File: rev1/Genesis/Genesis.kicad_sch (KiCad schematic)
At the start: 0 parts

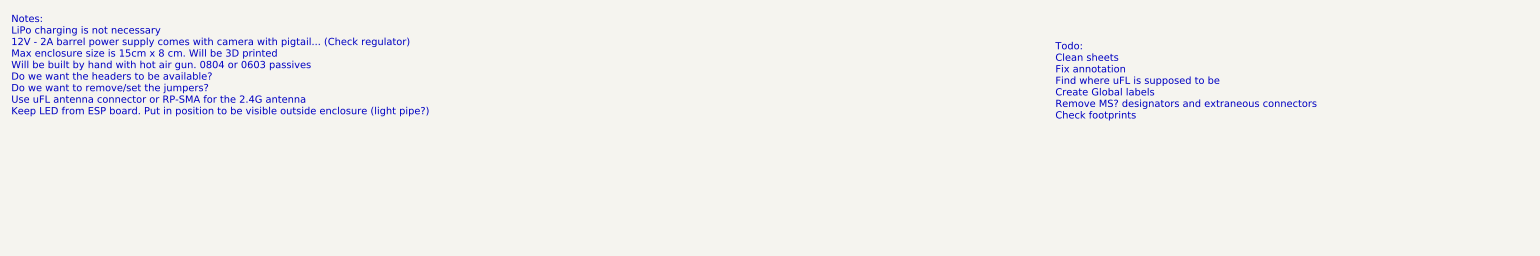
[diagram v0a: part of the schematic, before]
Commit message: Remove Stemma QT connectors and LiPo circuitry. Update Notes.
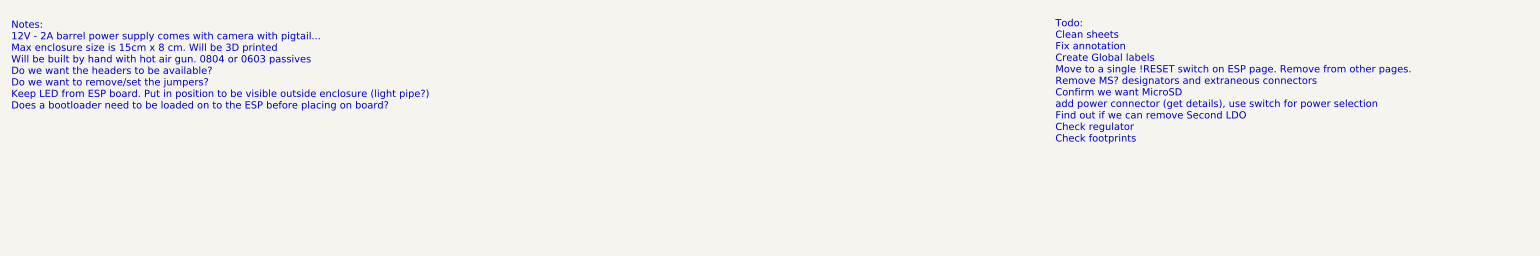
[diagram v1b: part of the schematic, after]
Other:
- note added: "Notes: 12V - 2A barrel power supply comes with camera with pigtail... Max enclosure size is 15cm x 8 cm. Will be 3D printed Will be built by hand with hot air gun. 0804 or 0603 passives Do we want the headers to be available? Do we want to remove/set the jumpers? Keep LED from ESP board. Put in position to be visible outside enclosure (light pipe?) Does a bootloader need to be loaded on to the ES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"
- note added: "Todo: Clean sheets Fix annotation Create Global labels Move to a single !RESET switch on ESP page. Remove from other pages. Remove MS? designators and extraneous connectors Confirm we want MicroSD add power connector (get details), use switch for power selection Find out if we can remove Second LDO Check regulator Check footprints"
- note removed: "Notes: LiPo charging is not necessary 12V - 2A barrel power supply comes with camera with pigtail... (Check regulator) Max enclosure size is 15cm x 8 cm. Will be 3D printed Will be built by hand with hot air gun. 0804 or 0603 passives Do we want the headers to be available? Do we want to remove/set the jumpers? Use uFL antenna connector or RP-SMA for the 2.4G antenna Keep LED from ESP board. Put 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"
- note removed: "Todo: Clean sheets Fix annotation Find where uFL is supposed to be Create Global labels Remove MS? designators and extraneous connectors Check footprints"
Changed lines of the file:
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@@
 		(company "Kingdom Metrics")
 	)
-	(text "Notes:\nLiPo charging is not necessary\n12V - 2A barrel power supply comes with camera with pigtail... (Check regulator)\nMax enclosure size is 15cm x 8 cm. Will be 3D printed\nWill be built by hand with hot air gun. 0804 or 0603 passives\nDo we want the headers to be available?\nDo we want to remove/set the jumpers?\nUse uFL antenna connector or RP-SMA for the 2.4G antenna\nKeep LED from ESP board. Put in position to be visible outside enclosure (light pipe?)"
+	(text "Notes:\n12V - 2A barrel power supply comes with camera with pigtail...\nMax enclosure size is 15cm x 8 cm. Will be 3D printed\nWill be built by hand with hot air gun. 0804 or 0603 passives\nDo we want the headers to be available?\nDo we want to remove/set the jumpers?\nKeep LED from ESP board. Put in position to be visible outside enclosure (light pipe?)\nDoes a bootloader need to be loaded on to the ESP before placing on board?"
 		(exclude_from_sim no)
 		(at 22.606 25.146 0)
@@
 		)
 	)
-	(text "Todo:\nClean sheets\nFix annotation\nFind where uFL is supposed to be\nCreate Global labels\nRemove MS? designators and extraneous connectors\nCheck footprints"
+	(text "Todo:\nClean sheets\nFix annotation\nCreate Global labels\nMove to a single !RESET switch on ESP page. Remove from other pages.  \nRemove MS? designators and extraneous connectors\nConfirm we want MicroSD\nadd power connector (get details), use switch for power selection\nFind out if we can remove Second LDO\nCheck regulator\nCheck footprints"
 		(exclude_from_sim no)
 		(at 207.772 27.94 0)

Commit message: Add initial annotation.
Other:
- note added: "Todo: Create Global labels Move to a single !RESET switch on ESP page. Remove from other pages. Remove MS? designators and extraneous connectors Confirm we want MicroSD add power connector (get details), use switch for power selection Find out if we can remove Second LDO Check regulator Check footprints"
- note removed: "Todo: Clean sheets Fix annotation Create Global labels Move to a single !RESET switch on ESP page. Remove from other pages. Remove MS? designators and extraneous connectors Confirm we want MicroSD add power connector (get details), use switch for power selection Find out if we can remove Second LDO Check regulator Check footprints"
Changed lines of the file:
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@@
 		)
 	)
-	(text "Todo:\nClean sheets\nFix annotation\nCreate Global labels\nMove to a single !RESET switch on ESP page. Remove from other pages.  \nRemove MS? designators and extraneous connectors\nConfirm we want MicroSD\nadd power connector (get details), use switch for power selection\nFind out if we can remove Second LDO\nCheck regulator\nCheck footprints"
+	(text "Todo:\nCreate Global labels\nMove to a single !RESET switch on ESP page. Remove from other pages.  \nRemove MS? designators and extraneous connectors\nConfirm we want MicroSD\nadd power connector (get details), use switch for power selection\nFind out if we can remove Second LDO\nCheck regulator\nCheck footprints"
 		(exclude_from_sim no)
 		(at 207.772 27.94 0)

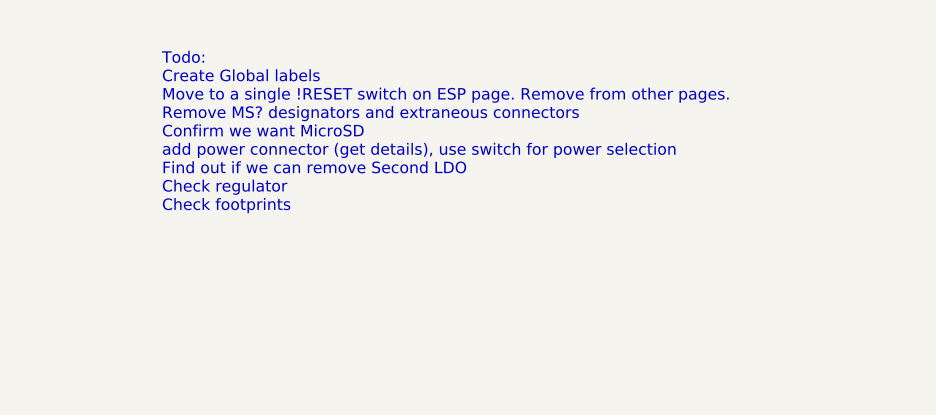
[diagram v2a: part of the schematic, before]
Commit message: Remove extra reset switches. Update notes.
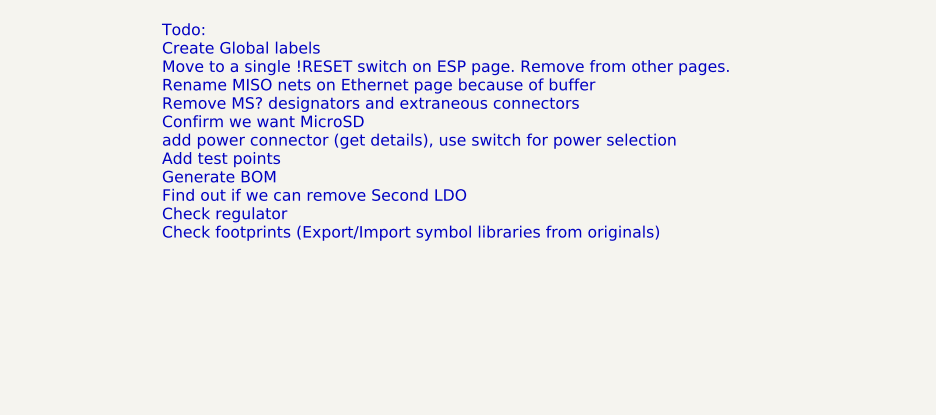
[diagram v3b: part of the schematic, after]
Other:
- note added: "Todo: Create Global labels Move to a single !RESET switch on ESP page. Remove from other pages. Rename MISO nets on Ethernet page because of buffer Remove MS? designators and extraneous connectors Confirm we want MicroSD add power connector (get details), use switch for power selection Add test points Generate BOM Find out if we can remove Second LDO Check regulator Check footprints (Export/Impor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"
- note removed: "Todo: Create Global labels Move to a single !RESET switch on ESP page. Remove from other pages. Remove MS? designators and extraneous connectors Confirm we want MicroSD add power connector (get details), use switch for power selection Find out if we can remove Second LDO Check regulator Check footprints"
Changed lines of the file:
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@@
 		)
 	)
-	(text "Todo:\nCreate Global labels\nMove to a single !RESET switch on ESP page. Remove from other pages.  \nRemove MS? designators and extraneous connectors\nConfirm we want MicroSD\nadd power connector (get details), use switch for power selection\nFind out if we can remove Second LDO\nCheck regulator\nCheck footprints"
+	(text "Todo:\nCreate Global labels\nMove to a single !RESET switch on ESP page. Remove from other pages.\nRename MISO nets on Ethernet page because of buffer \nRemove MS? designators and extraneous connectors\nConfirm we want MicroSD\nadd power connector (get details), use switch for power selection\nAdd test points\nGenerate BOM\nFind out if we can remove Second LDO\nCheck regulator\nCheck footprints (Export/Import symbol libraries from originals)"
 		(exclude_from_sim no)
 		(at 207.772 27.94 0)

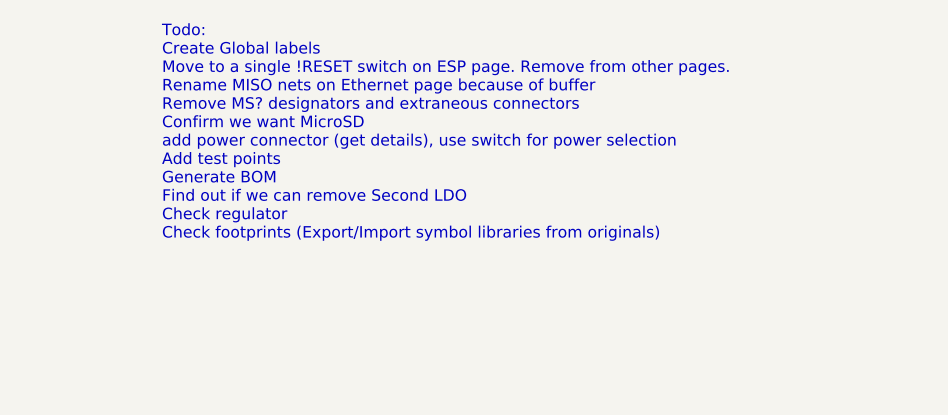
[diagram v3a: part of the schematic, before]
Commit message: Update todo list and pdf schematic.
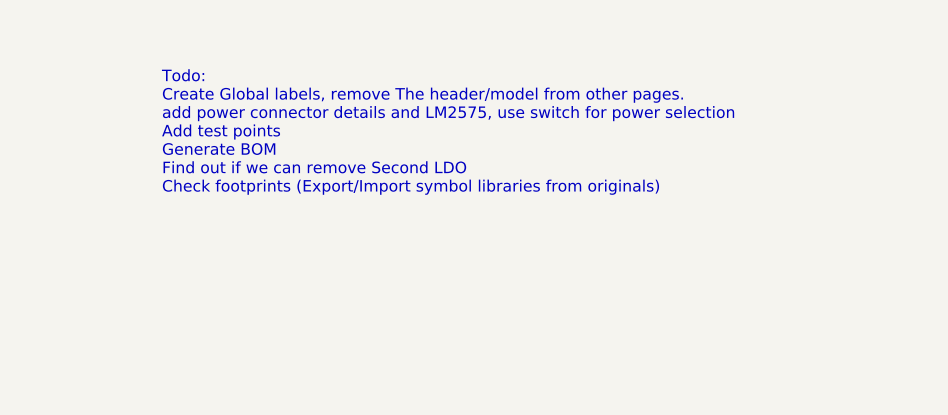
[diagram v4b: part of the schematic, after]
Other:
- note added: "Todo: Create Global labels, remove The header/model from other pages. add power connector details and LM2575, use switch for power selection Add test points Generate BOM Find out if we can remove Second LDO Check footprints (Export/Import symbol libraries from originals)"
- note removed: "Todo: Create Global labels Move to a single !RESET switch on ESP page. Remove from other pages. Rename MISO nets on Ethernet page because of buffer Remove MS? designators and extraneous connectors Confirm we want MicroSD add power connector (get details), use switch for power selection Add test points Generate BOM Find out if we can remove Second LDO Check regulator Check footprints (Export/Impor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"
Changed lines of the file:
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@@
 		)
 	)
-	(text "Todo:\nCreate Global labels\nMove to a single !RESET switch on ESP page. Remove from other pages.\nRename MISO nets on Ethernet page because of buffer \nRemove MS? designators and extraneous connectors\nConfirm we want MicroSD\nadd power connector (get details), use switch for power selection\nAdd test points\nGenerate BOM\nFind out if we can remove Second LDO\nCheck regulator\nCheck footprints (Export/Import symbol libraries from originals)"
+	(text "Todo:\nCreate Global labels, remove The header/model from other pages.\nadd power connector details and LM2575, use switch for power selection\nAdd test points\nGenerate BOM\nFind out if we can remove Second LDO\nCheck footprints (Export/Import symbol libraries from originals)"
 		(exclude_from_sim no)
 		(at 207.772 27.94 0)

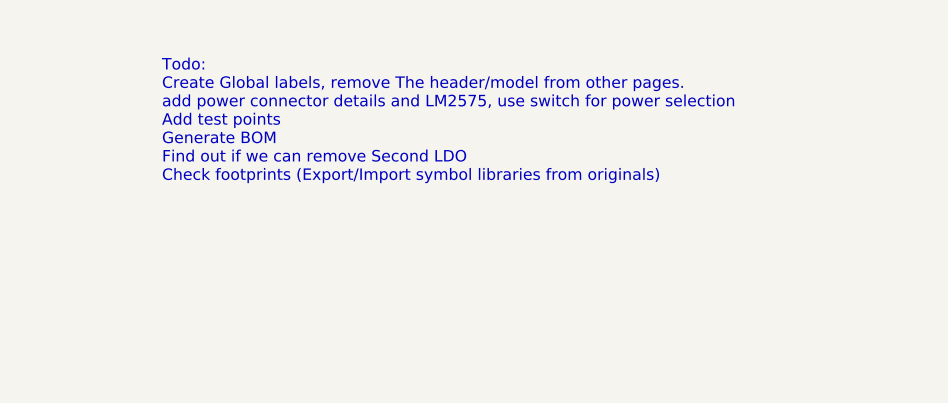
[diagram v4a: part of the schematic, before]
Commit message: Remove second LDO. Power Neopixel from main 3.3.
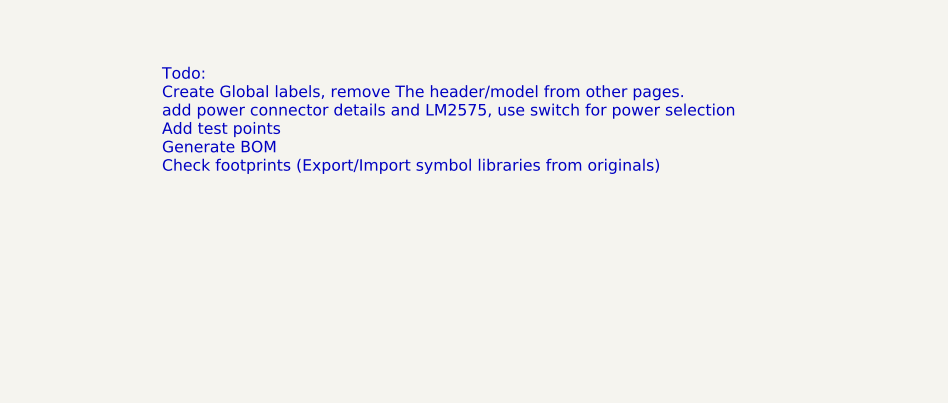
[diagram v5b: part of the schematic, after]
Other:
- note added: "Todo: Create Global labels, remove The header/model from other pages. add power connector details and LM2575, use switch for power selection Add test points Generate BOM Check footprints (Export/Import symbol libraries from originals)"
- note removed: "Todo: Create Global labels, remove The header/model from other pages. add power connector details and LM2575, use switch for power selection Add test points Generate BOM Find out if we can remove Second LDO Check footprints (Export/Import symbol libraries from originals)"
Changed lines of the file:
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@@
 		)
 	)
-	(text "Todo:\nCreate Global labels, remove The header/model from other pages.\nadd power connector details and LM2575, use switch for power selection\nAdd test points\nGenerate BOM\nFind out if we can remove Second LDO\nCheck footprints (Export/Import symbol libraries from originals)"
+	(text "Todo:\nCreate Global labels, remove The header/model from other pages.\nadd power connector details and LM2575, use switch for power selection\nAdd test points\nGenerate BOM\nCheck footprints (Export/Import symbol libraries from originals)"
 		(exclude_from_sim no)
 		(at 207.772 27.94 0)

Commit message: Add note to check VDD pins on usb to serial convertor.
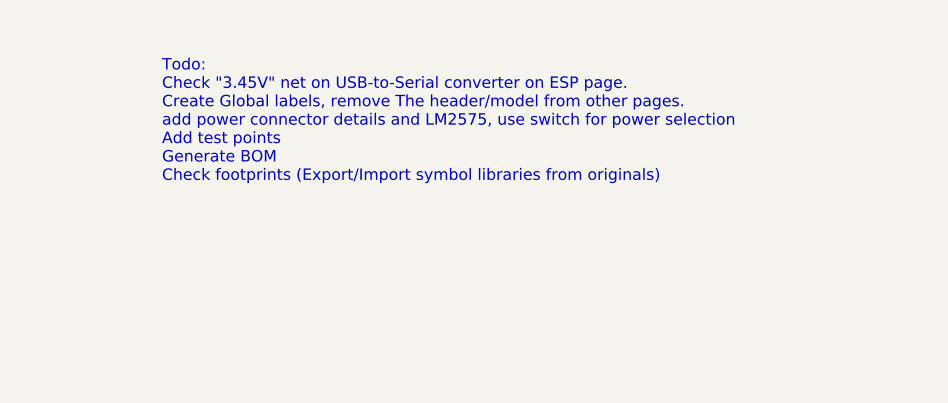
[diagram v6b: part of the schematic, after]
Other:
- note added: "Todo: Check "3.45V" net on USB-to-Serial converter on ESP page. Create Global labels, remove The header/model from other pages. add power connector details and LM2575, use switch for power selection Add test points Generate BOM Check footprints (Export/Import symbol libraries from originals)"
- note removed: "Todo: Create Global labels, remove The header/model from other pages. add power connector details and LM2575, use switch for power selection Add test points Generate BOM Check footprints (Export/Import symbol libraries from originals)"
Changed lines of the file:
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@@
 		)
 	)
-	(text "Todo:\nCreate Global labels, remove The header/model from other pages.\nadd power connector details and LM2575, use switch for power selection\nAdd test points\nGenerate BOM\nCheck footprints (Export/Import symbol libraries from originals)"
+	(text "Todo:\nCheck \"3.45V\" net on USB-to-Serial converter on ESP page.\nCreate Global labels, remove The header/model from other pages.\nadd power connector details and LM2575, use switch for power selection\nAdd test points\nGenerate BOM\nCheck footprints (Export/Import symbol libraries from originals)"
 		(exclude_from_sim no)
 		(at 207.772 27.94 0)
